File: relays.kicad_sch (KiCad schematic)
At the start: 5 parts, among them U3 BTS716GB

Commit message: Digital IO, Relay, and Switchbox changes
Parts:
- removed D3, D4, D5, D6: D, RRE02VTM4SFHTR:DIO_RRE02VSM_ROM, symbol Device:D
- removed U3: BTS716GB, BTS716GB:SOIC127P1032X265-20N, symbol BTS716GB:BTS716GB
- added J6, J7, J8, J9: 2-1445057-2, 2-1445057-2:TE_2-1445057-2, symbol 2-1445057-2:2-1445057-2
- added K1, K2, K3, K4: J107F1AS123VDC.36, J107F1AS123VDC.36:RELAY_J107F1AS123VDC.36, symbol J107F1AS123VDC.36:J107F1AS123VDC.36
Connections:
- net BattRelay: now also K4.COIL1
- net ExtraRelay: now also K3.COIL1
- net GND: now also K1.COIL2, K2.COIL2, K3.COIL2, K4.COIL2
- net LeftTurnSignal: now also K2.COIL1
- net RightTurnSignal: now also K1.COIL1
- new net: J6.1, K4.NO
- new net: J6.2, K4.COM
- new net +12V: J7.1, J8.1, J9.1, K1.NO, K2.NO, K3.NO
- new net GNDp: J7.2, J8.2, J9.2, K1.COM, K2.COM, K3.COM
- no-connect marks 2 -> 0

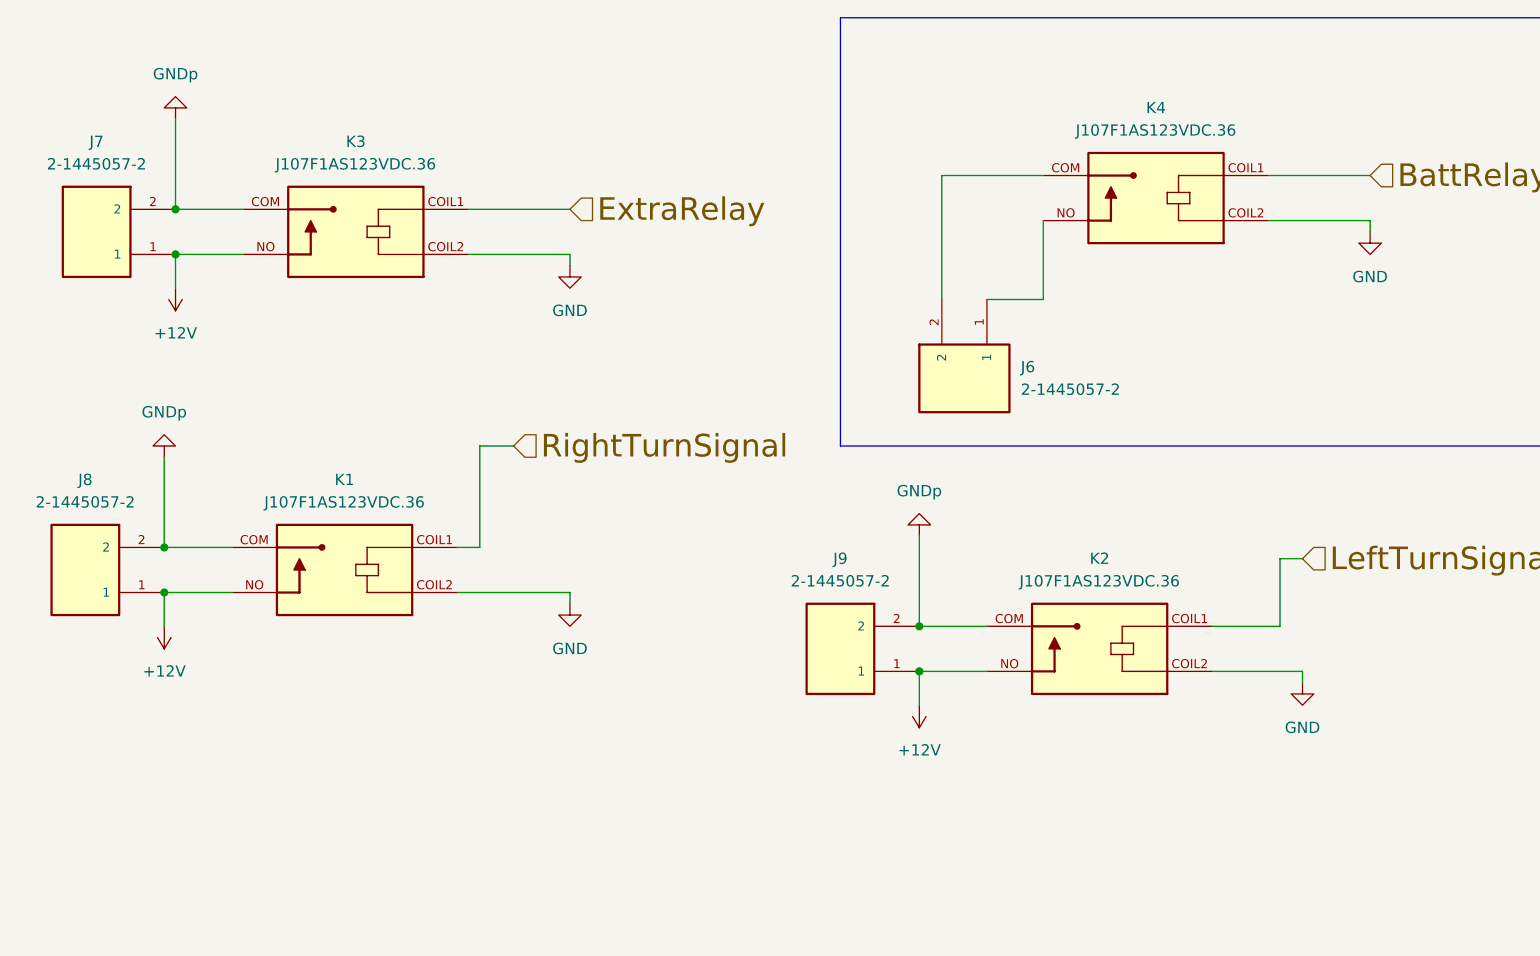
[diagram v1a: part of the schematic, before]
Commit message: Fixed Relay output to not short +12V
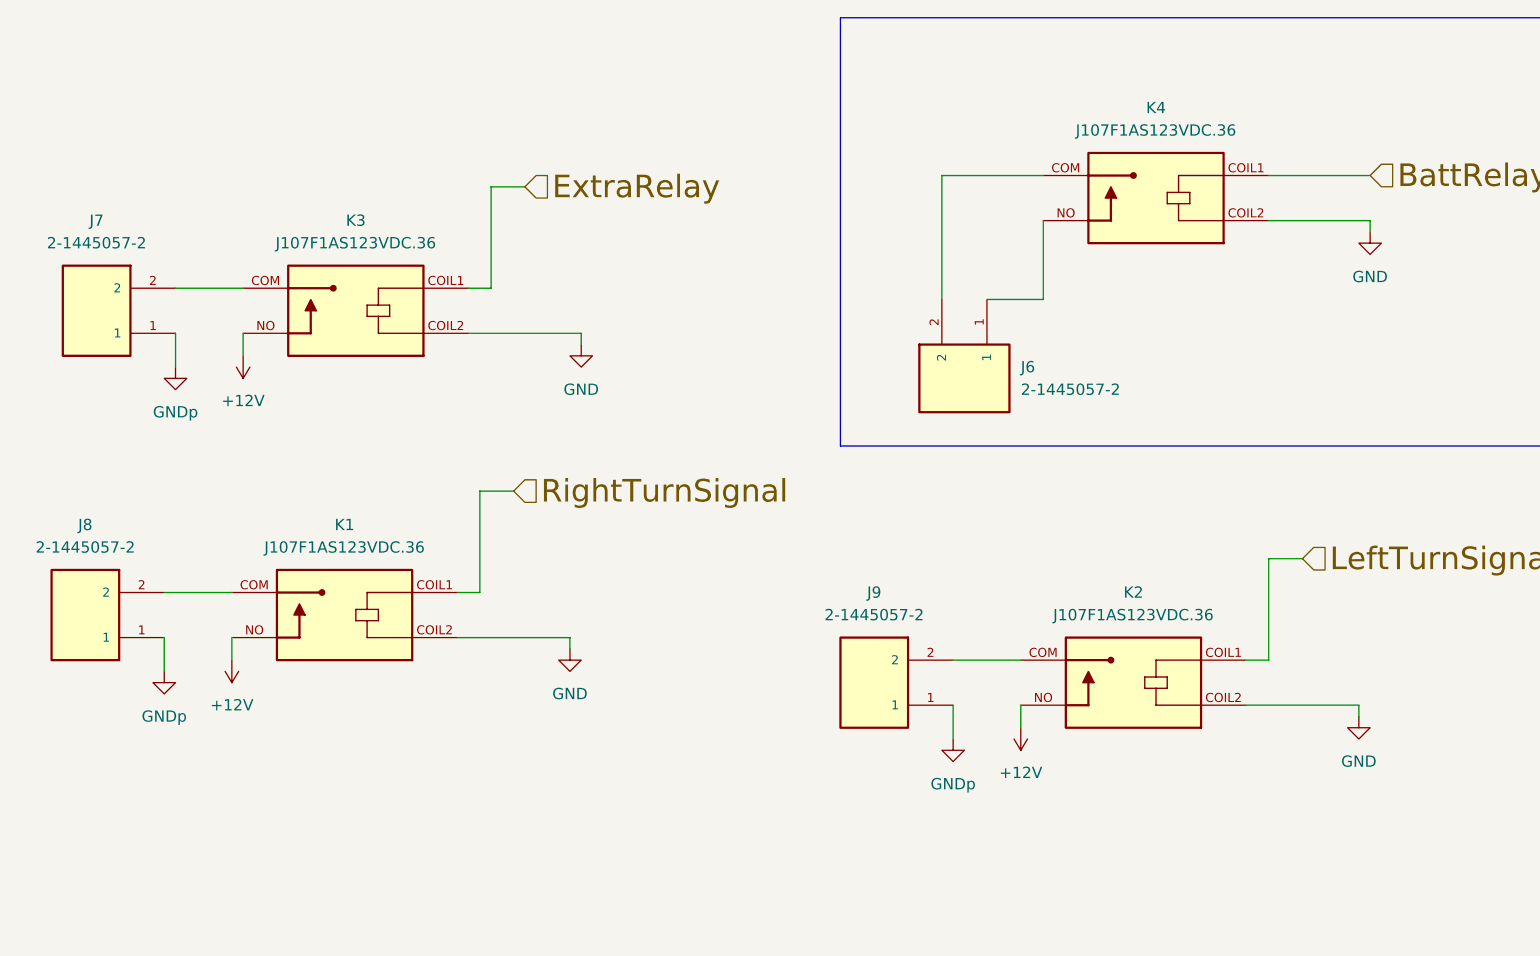
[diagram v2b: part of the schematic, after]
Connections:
- net +12V: no longer J7.1, J8.1, J9.1
- net GNDp: now also J7.1, J8.1, J9.1; no longer J7.2, J8.2, J9.2, K1.COM, K2.COM, K3.COM
- new net: J9.2, K2.COM
- new net: J8.2, K1.COM
- new net: J7.2, K3.COM
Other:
- moved on the sheet: J8, K1

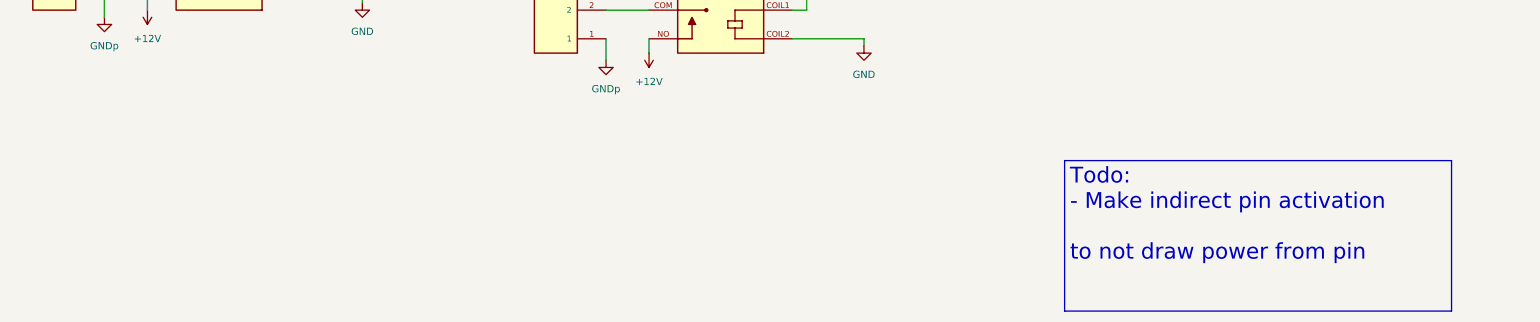
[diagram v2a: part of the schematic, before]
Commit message: Added Analog inputs
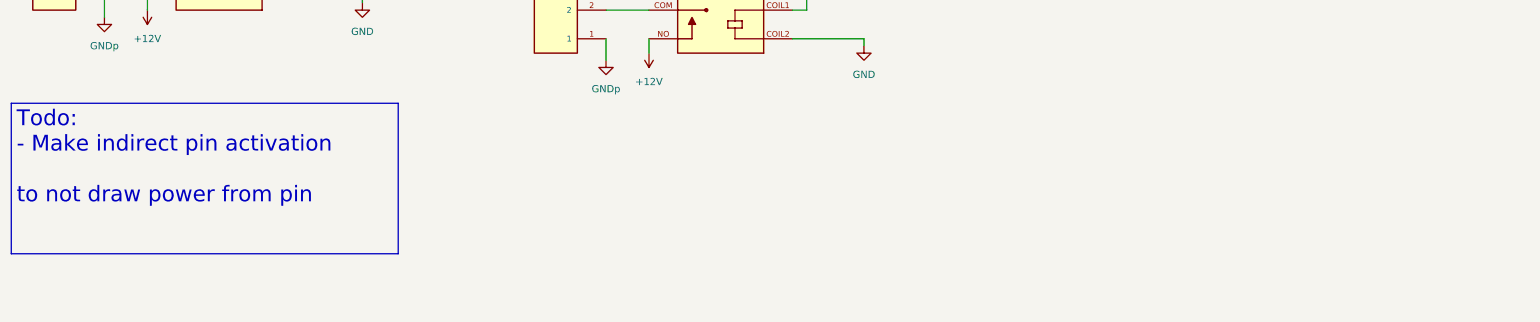
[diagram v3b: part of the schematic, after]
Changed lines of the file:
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@@
 	(text_box "Todo:\n- Make indirect pin activation \n  to not draw power from pin"
 		(exclude_from_sim no)
-		(at 204.47 111.76 0)
+		(at 17.78 101.6 0)
 		(size 68.58 26.67)
 		(margins 0.9525 0.9525 0.9525 0.9525)

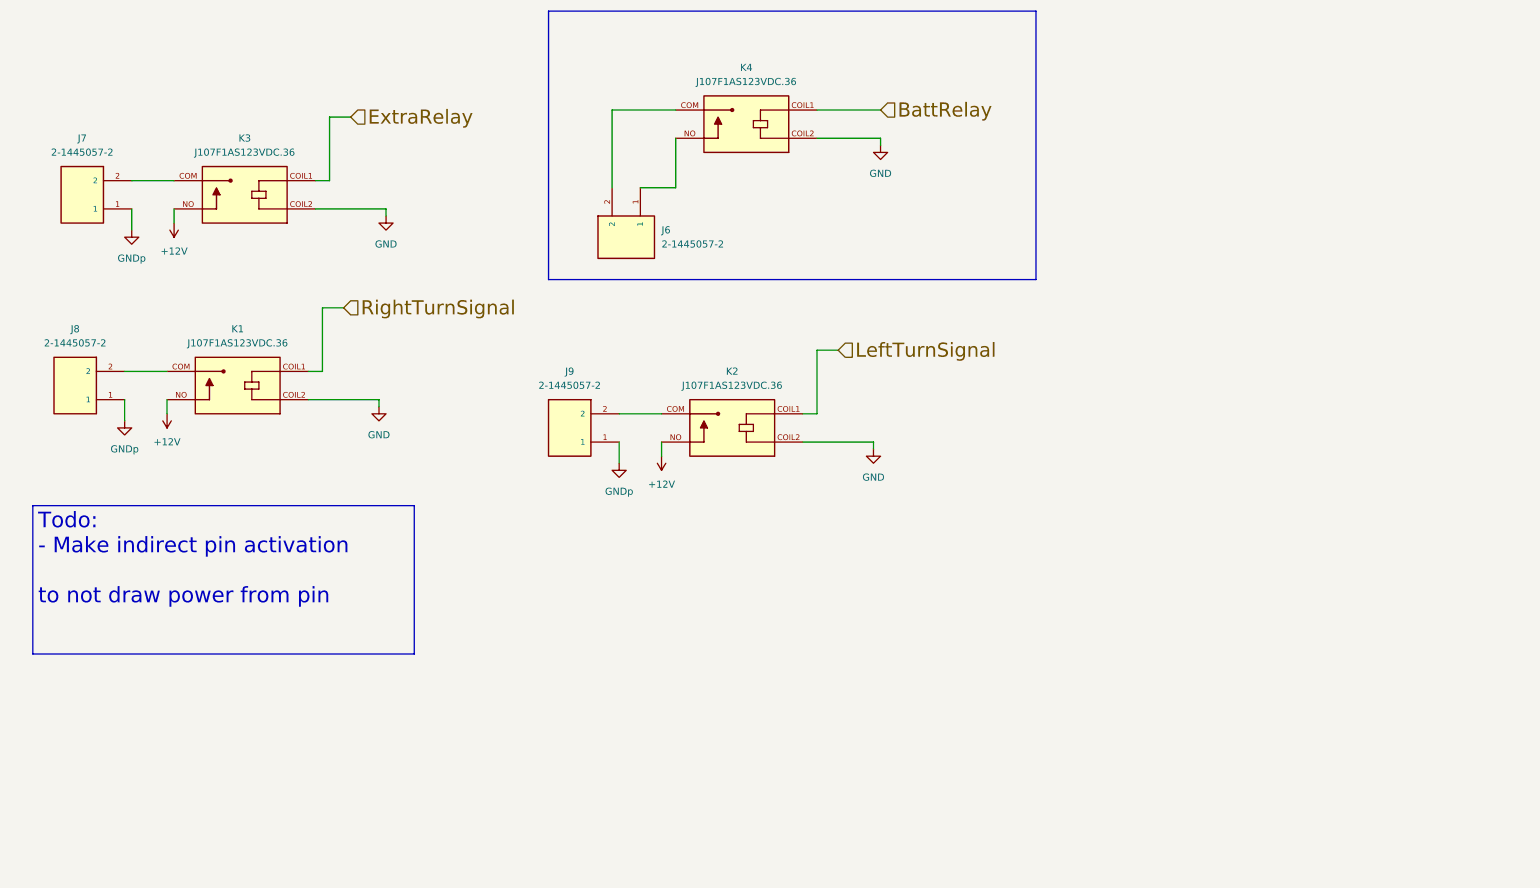
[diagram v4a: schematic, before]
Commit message: Added transistor to control relays
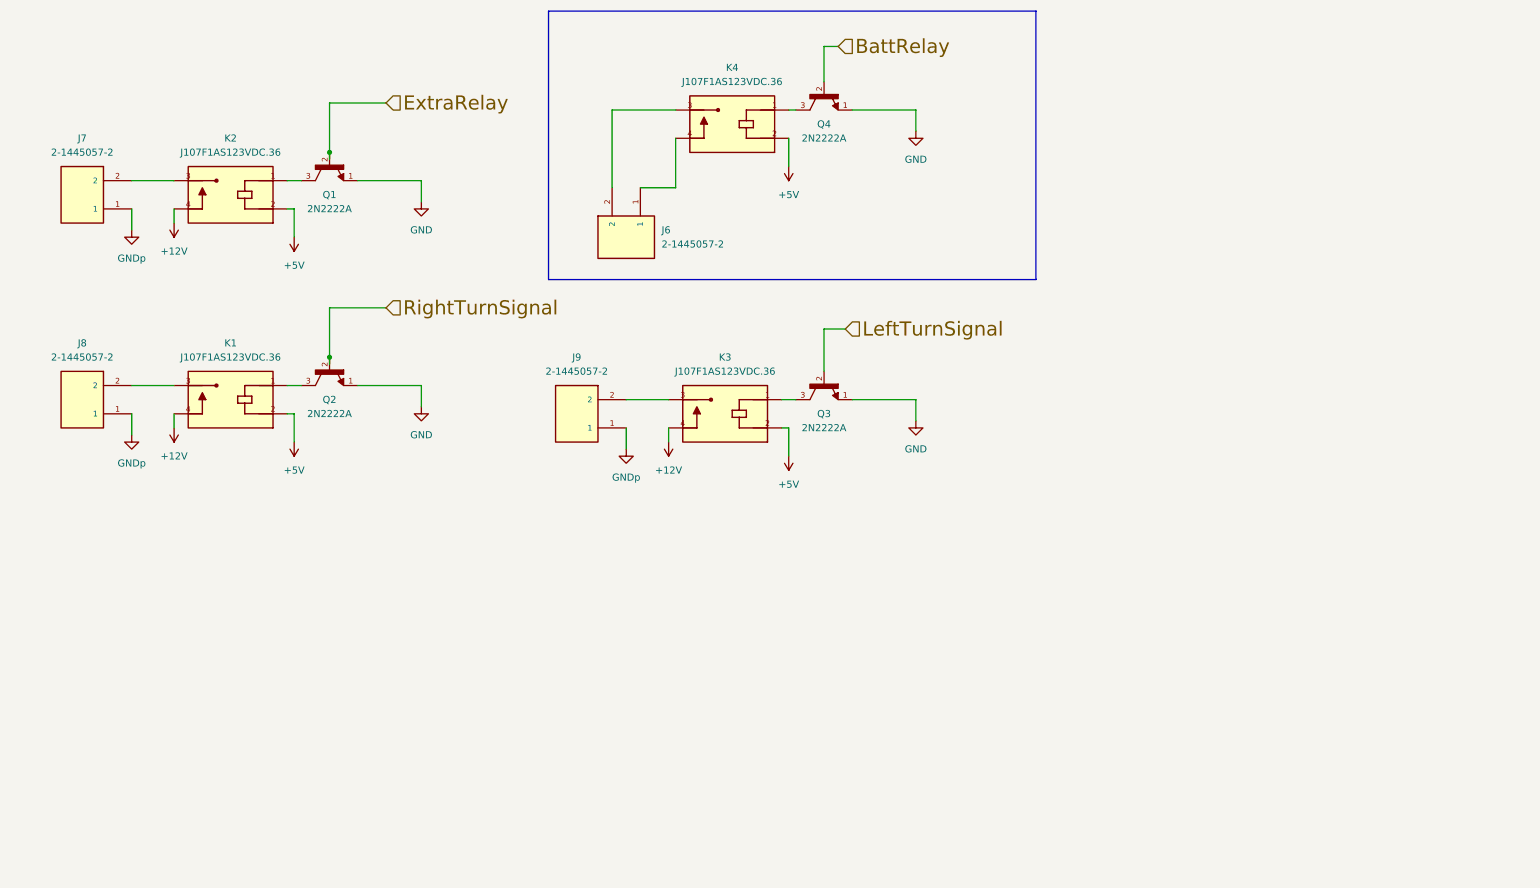
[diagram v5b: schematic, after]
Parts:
- removed K1, K2, K3, K4: J107F1AS123VDC.36, J107F1AS123VDC.36:RELAY_J107F1AS123VDC.36, symbol J107F1AS123VDC.36:J107F1AS123VDC.36
- added K1, K2, K3, K4: J107F1AS123VDC.36, PRE29-5V-S-450-1A-E:RELAY_PRE29-5V-S-450-1A-E, symbol PRE29-5V-S-450-1A-E:PRE29-5V-S-450-1A-E
- added Q1, Q2, Q3, Q4: 2N2222A, 2N2222A:TO92254P470H750-3, symbol 2N2222A:2N2222A
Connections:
- net +12V: now also K1.4, K2.4, K3.4
- net BattRelay: now also Q4.2
- net ExtraRelay: now also Q1.2
- net GND: now also Q1.1, Q2.1, Q3.1, Q4.1
- net LeftTurnSignal: now also Q3.2
- net RightTurnSignal: now also Q2.2
- net at J9.2: now also K3.3
- net at J8.2: now also K1.3
- net at J7.2: now also K2.3
- net at J6.1: now also K4.4
- net at J6.2: now also K4.3
- new net: K3.1, Q3.3
- new net: K4.1, Q4.3
- new net: K2.1, Q1.3
- new net: K1.1, Q2.3
- new net +5V: K1.2, K2.2, K3.2, K4.2

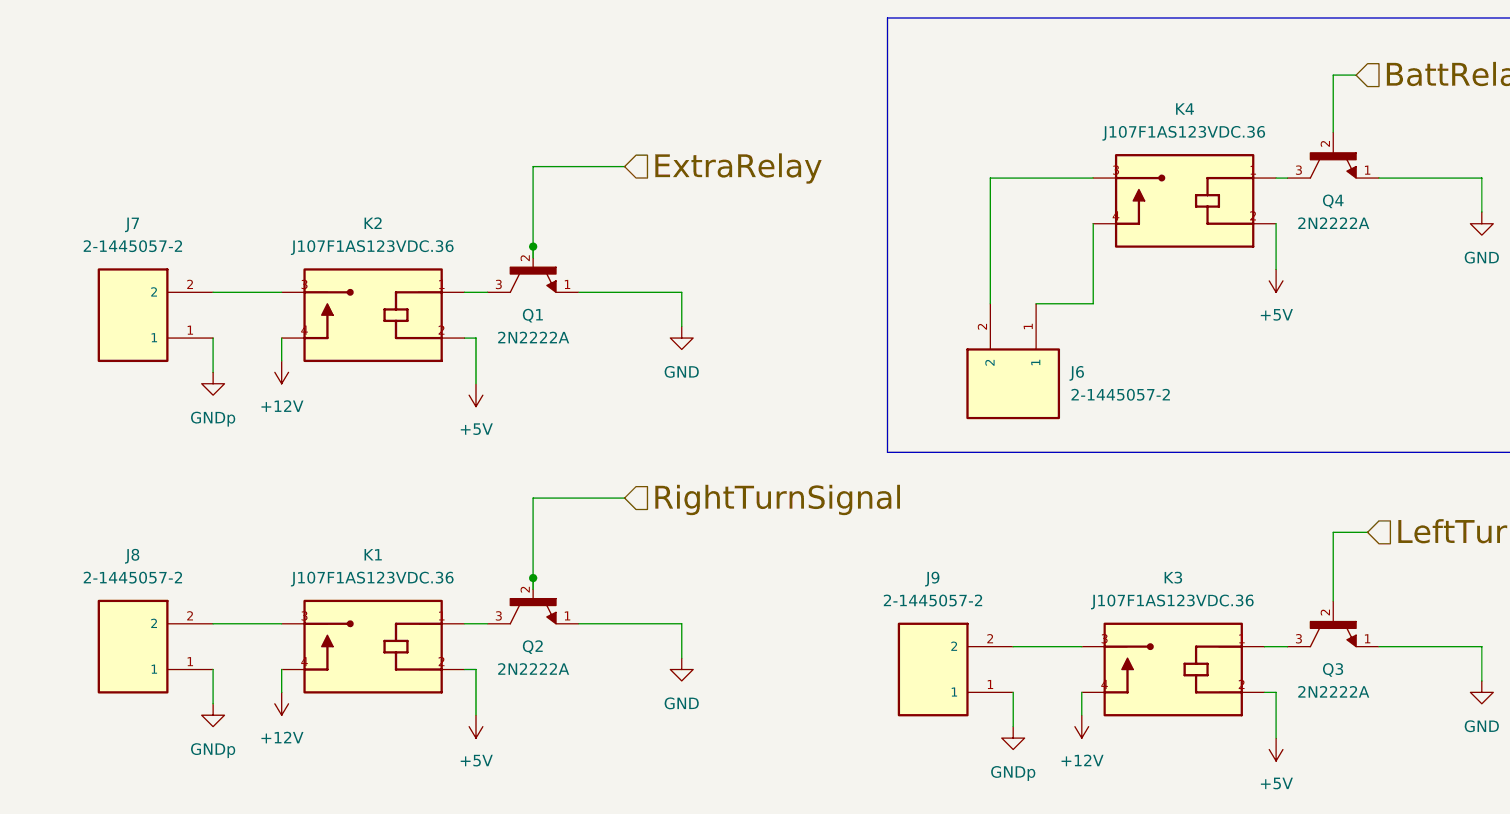
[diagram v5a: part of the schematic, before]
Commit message: Moved everything to 23-POS AmpSeal
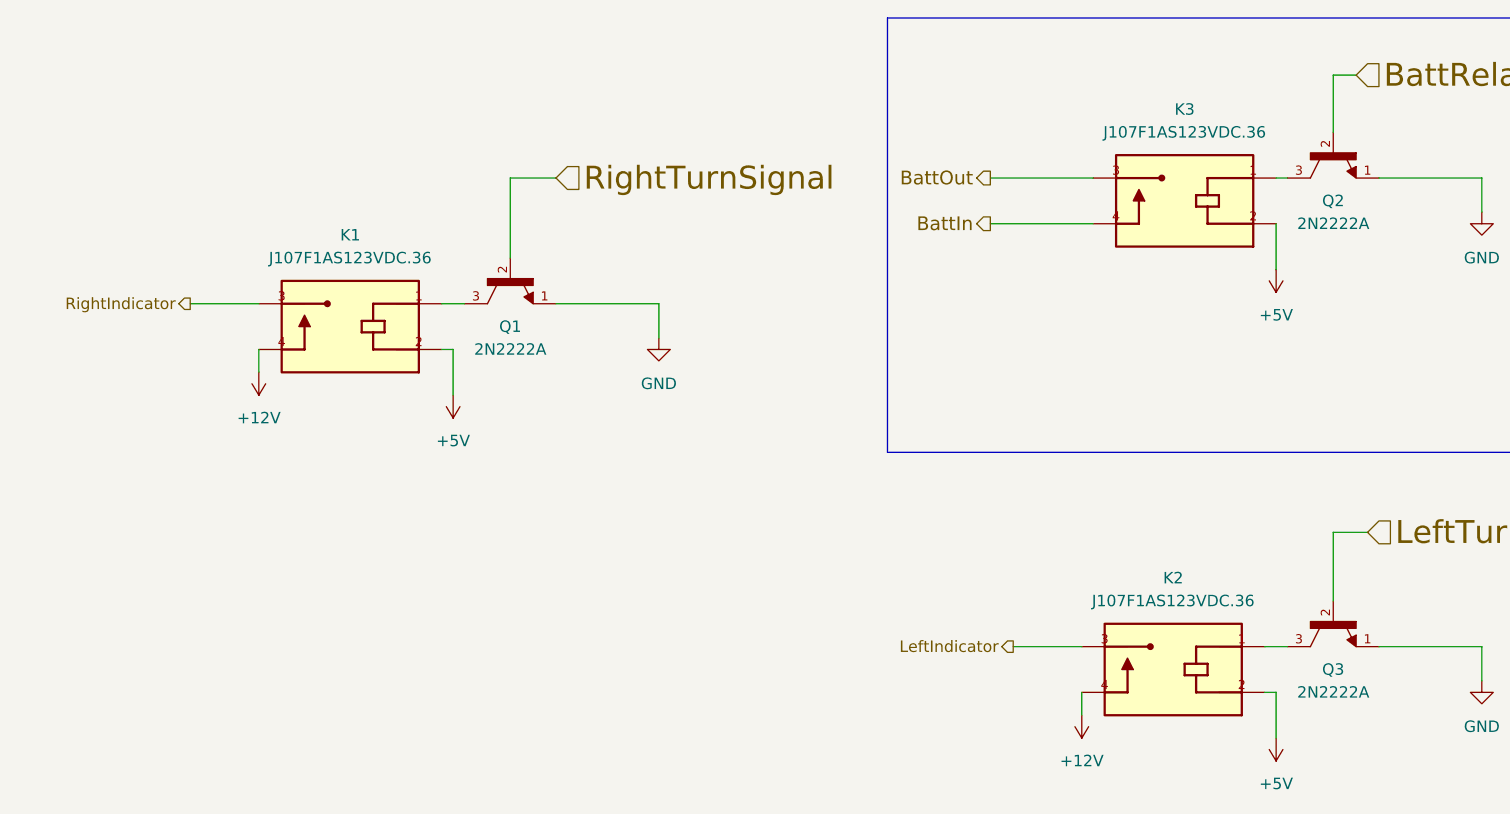
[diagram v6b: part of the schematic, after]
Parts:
- removed J6, J7, J8, J9: 2-1445057-2, 2-1445057-2:TE_2-1445057-2, symbol 2-1445057-2:2-1445057-2
- removed K2: J107F1AS123VDC.36, PRE29-5V-S-450-1A-E:RELAY_PRE29-5V-S-450-1A-E, symbol PRE29-5V-S-450-1A-E:PRE29-5V-S-450-1A-E
- removed Q1: 2N2222A, 2N2222A:TO92254P470H750-3, symbol 2N2222A:2N2222A
- renumbered K3 to K2, K4 to K3, Q2 to Q1, Q4 to Q2
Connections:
- net BattIn: now reaches K3.4
- net BattOut: now reaches K3.3
- net RightIndicator: now reaches K1.3
- net LeftIndicator: now reaches K2.3
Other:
- moved on the sheet: K1, Q1
